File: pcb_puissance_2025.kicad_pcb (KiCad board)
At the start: 2 copper layers, 150 x 90 mm, 120 parts, among them J1 1755736, J10 1755736, J12 1755736, J13 1755736, J14 Conn_02x06_Odd_Even, J15 1755736, J16 1755736, J17 Conn_02x06_Odd_Even, J18 1755736, J19 1755736, J2 1755736, J20 Conn_02x06_Odd_Even, J21 1755736, J22 1755736, J3 1755736, J4 1755736, J5 1755736, J6 1755736, J7 Conn_02x10_Odd_Even, J8 Conn_ST_STDC14, J9 12402012E212A, Q1 SUD50P06-15, Q2 SUD50P06-15, Q3 SUD50P06-15, Q4 SUD50P06-15, Q5 SUD50P06-15, Q6 SUD50P06-15, Q7 STL40DN3LLH5, Q8 NPN, SW1 SW_Push, U1 LTC4417IGN, U10 MCP9808T-E/MS, U2 STM32G491KEU6, U3 INA236BIDDFR, U4 INA236AIDDFR, U5 INA236AIDDFR, U6 INA236AIDDFR, U7 INA236BIDDFR, U8 INA236BIDDFR, U9 TCPP02-M18

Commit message: PCB 2025 rev2
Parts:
- removed J9: 12402012E212A, Modelec:AMPHENOL_12402012E212A
- added J11: USB_C_Receptacle_USB2.0_16P, Modelec:GCT_USB4105-GF-A, B.Cu at (144.2, 145.4)
- added R29: 2k2, Resistor_SMD:R_0805_2012Metric_Pad1.20x1.40mm_HandSolder, B.Cu at (204.4, 141.9)
- added R30: 2k2, Resistor_SMD:R_0805_2012Metric_Pad1.20x1.40mm_HandSolder, B.Cu at (199.8, 141.9)
- added TP1: TestPoint, TestPoint:TestPoint_Pad_D1.5mm, B.Cu at (186.8, 100.0)
- added TP10: TestPoint, TestPoint:TestPoint_Bridge_Pitch2.0mm_Drill0.7mm, B.Cu at (223.5, 74.5)
- added TP2: TestPoint, TestPoint:TestPoint_Pad_D1.5mm, B.Cu at (158.5, 92.0)
- added TP3: TestPoint, TestPoint:TestPoint_Pad_D1.5mm, B.Cu at (189.6, 136.4)
- added TP4: TestPoint, TestPoint:TestPoint_Pad_D1.5mm, B.Cu at (166.5, 79.0)
- added TP5: TestPoint, TestPoint:TestPoint_Pad_D1.5mm, B.Cu at (166.5, 86.5)
- added TP6: TestPoint, TestPoint:TestPoint_Pad_D1.5mm, B.Cu at (166.5, 94.0)
- added TP7: TestPoint, TestPoint:TestPoint_Pad_D1.5mm, B.Cu at (166.5, 101.5)
- added TP8: TestPoint, TestPoint:TestPoint_Pad_D1.5mm, B.Cu at (166.5, 109.0)
- added TP9: TestPoint, TestPoint:TestPoint_Bridge_Pitch2.0mm_Drill0.7mm, B.Cu at (215.5, 72.5)
- C1, C3, C5: value 0.4u -> 0u4
- C11: value 4.7u -> 4u7
- C22: value 2.2u -> 2u2
- R10, R7: value 37.4k -> 37k4
- R11, R8: value 78.7k -> 78k7
- R13, R14, R15: value 8.06k -> 8k06
- R19: value L4CL1206LR013DNR -> 62m 0.5%
- R20, R22: value L4CL1206LR013DNR -> 13m 0.5%
- R21: value L4CL1206LR013DNR -> 20m 0.5%
- R23, R24: value 4m -> 4m 0.5%
- R25: value L4CL1206LR007FNR -> 7m 1%
- R4: value 63.4k -> 63k4
- moved REF** 13.0 mm to (186.0, 84.8)
- moved C23 3.64 mm to (140.2, 88.5), turned to -90 degrees
- moved Q8 0.85 mm to (171.6, 115.8)
- moved R27 0.85 mm to (170.6, 119.5)
- renumbered F6 to F5, F5 to F6
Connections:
- net /Microcontroller/12VALERT renamed /Microcontroller/24VALERT
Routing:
- net GND: track 59.2 -> 117.3 mm, vias 720 -> 743
- net /Microcontroller/SCL: track 296.8 -> 312.5 mm, vias 19 -> 20
- net /3V3: track 378.5 -> 390.7 mm, vias 27 -> 33
- net /Microcontroller/SDA: track 293.7 -> 305.4 mm, vias 17 -> 18
- net Net-(PS1-+VIN_(VCC)): track 21.9 -> 24.2 mm, vias 0 -> 1
- net Net-(BZ1-+): track 5.20 -> 6.30 mm
- net Net-(J11-CC2): track 5.94 -> 6.97 mm
- net /Microcontroller/EMG_PUSHED: track 195.2 -> 196.1 mm
- net Net-(R27-Pad1): track 6.68 -> 7.53 mm
- net Net-(U5-IN-): track 5.12 -> 5.66 mm
- net Net-(U5-IN+): track 5.14 -> 5.68 mm
- net /power_input_selector/VOUT: track 3.47 -> 3.56 mm, vias 1 -> 2
- net Net-(PS3-+VIN_(VCC)): vias 0 -> 1
- net Net-(PS5-+VIN_(VCC)): vias 0 -> 1
- net Net-(PS4-+VIN_(VCC)): vias 0 -> 1
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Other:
- board text added: "12V FUSE"
- board text added: "24V FUSE"
- board text added: "3V3 FUSE"
- board text added: "5V FUSE"
- board text added: "5V15 FUSE"
- board text added: "BUZZER ACTIVATE"
- board text added: "SCL"
- board text added: "SDA"
- board text added: "VIN"
- board text removed: "BIBERON V1 - MARCEL"

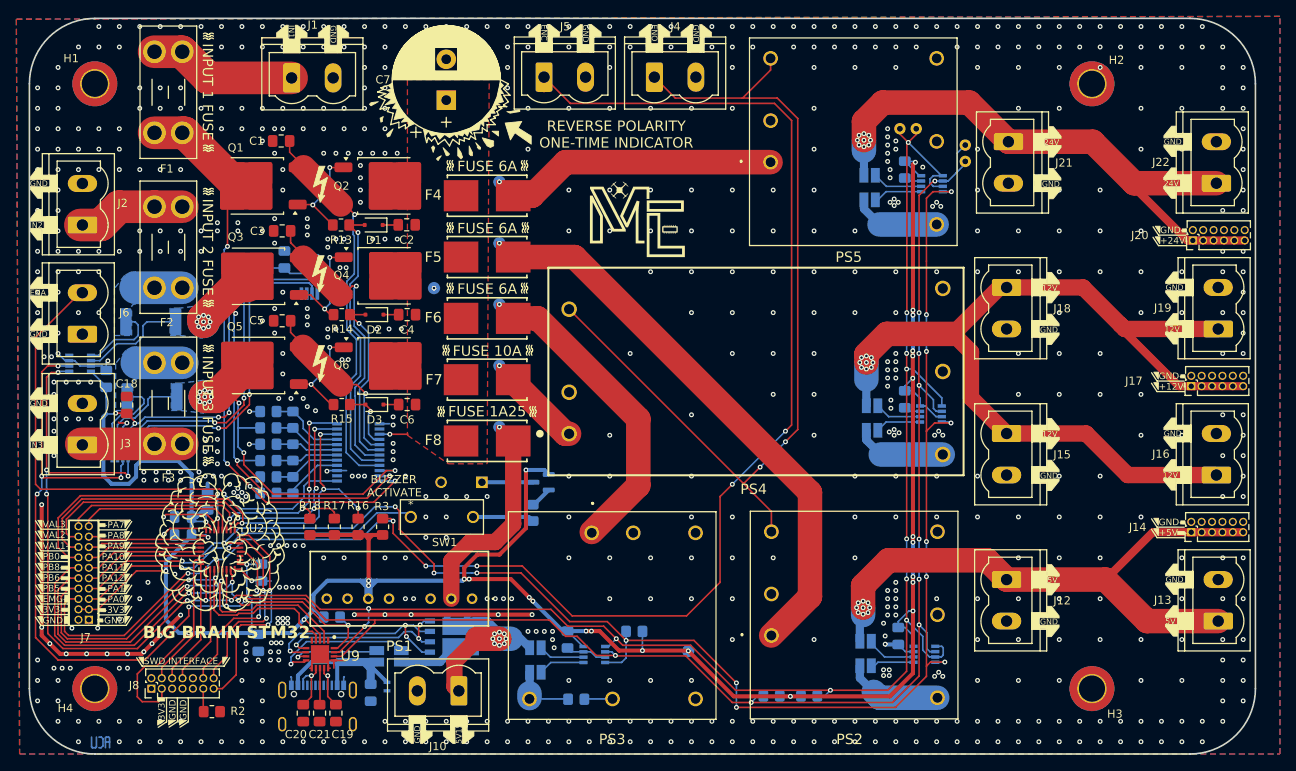
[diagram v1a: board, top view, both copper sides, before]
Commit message: nouvelle version : correction erreurs, ameliorations qualite, passage a 4 couches, ajout pilotage des traco depuis le stm32
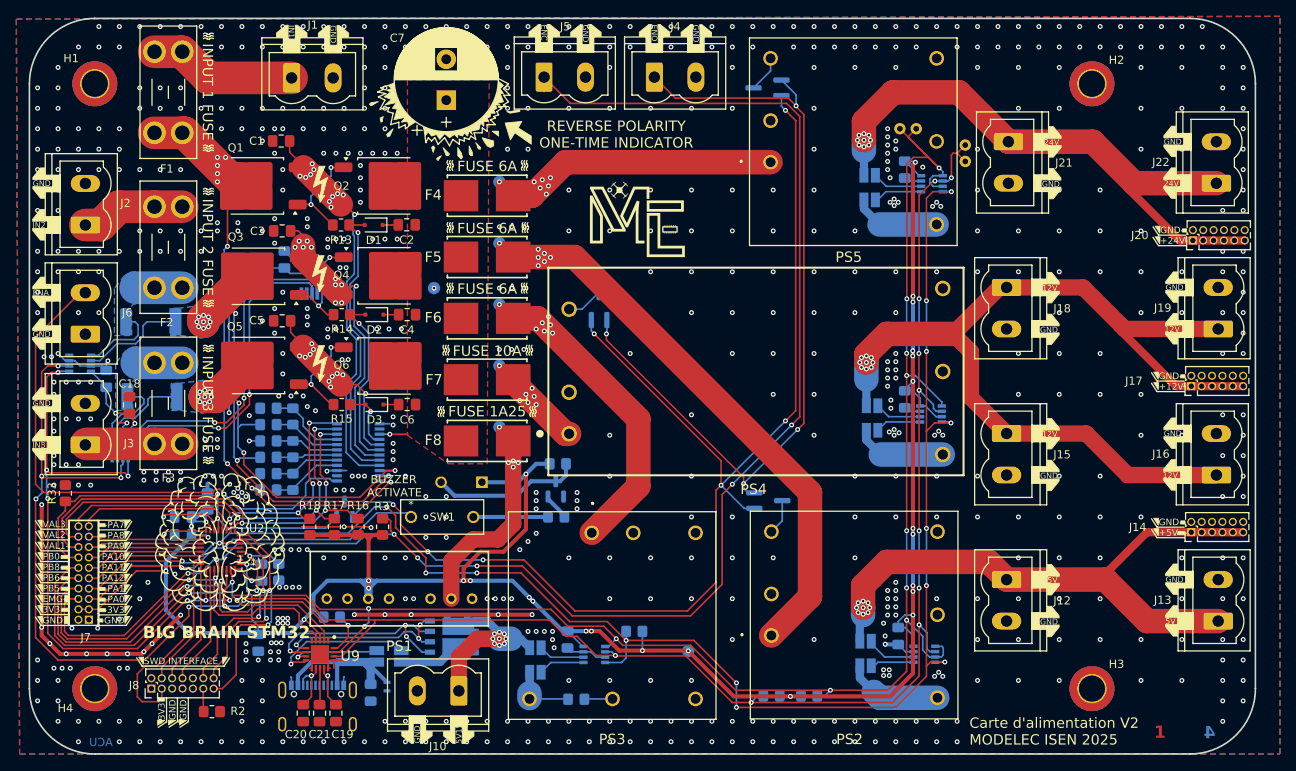
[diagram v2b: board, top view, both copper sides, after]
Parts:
- added D5: D_Dual_CommonAnode_AKK_Parallel, Package_TO_SOT_SMD:TSOT-23_HandSoldering, B.Cu at (199.4, 118.0)
- added D6: D_Dual_CommonAnode_AKK_Parallel, Package_TO_SOT_SMD:TSOT-23_HandSoldering, B.Cu at (178.7, 94.2)
- added D7: D_Dual_CommonAnode_AKK_Parallel, Package_TO_SOT_SMD:TSOT-23_HandSoldering, B.Cu at (199.3, 67.5)
- added Q9: NMOS, Package_TO_SOT_SMD:SOT-23, B.Cu at (147.6, 119.1)
- added R31: 1k, Resistor_SMD:R_0805_2012Metric_Pad1.20x1.40mm_HandSolder, B.Cu at (173.7, 113.5)
- added R32: 1k, Resistor_SMD:R_0805_2012Metric_Pad1.20x1.40mm_HandSolder, B.Cu at (139.5, 126.8)
- added R33: 1k, Resistor_SMD:R_0805_2012Metric_Pad1.20x1.40mm_HandSolder, F.Cu at (113.4, 117.1)
- added REF**: Symbol_HighVoltage_NoTriangle_2x5mm_Copper, Symbol:Symbol_HighVoltage_NoTriangle_2x5mm_Copper, F.Cu at (175.3, 73.4)
- added REF**: Symbol_HighVoltage_NoTriangle_2x5mm_Copper, Symbol:Symbol_HighVoltage_NoTriangle_2x5mm_Copper, F.Cu at (182.3, 71.4)
- added REF**: Symbol_HighVoltage_NoTriangle_2x5mm_Copper, Symbol:Symbol_HighVoltage_NoTriangle_2x5mm_Copper, B.Cu at (174.3, 76.4)
- added REF**: Symbol_HighVoltage_NoTriangle_2x5mm_Copper, Symbol:Symbol_HighVoltage_NoTriangle_2x5mm_Copper, B.Cu at (179.3, 70.4)
- C7: footprint Capacitor_THT:CP_Radial_D13.0mm_P5.00mm -> Capacitor_THT:CP_Radial_D12.5mm_P5.00mm
- moved R27 2.89 mm to (173.4, 120.0), turned to 0 degrees
- moved Q8 1.97 mm to (173.4, 116.6), turned to 90 degrees
- moved REF** 1.88 mm to (187.3, 86.2)
- moved R10 0.40 mm to (138.2, 106.7)
- moved R11 0.40 mm to (141.2, 107.7)
- moved R12 0.40 mm to (138.2, 108.7)
- moved R4 0.40 mm to (138.2, 114.7)
- moved R5 0.40 mm to (141.2, 115.7)
- moved R6 0.40 mm to (138.2, 116.7)
- moved R7 0.40 mm to (138.2, 110.7)
- moved R8 0.40 mm to (141.2, 111.7)
- moved R9 0.40 mm to (138.2, 112.7)
- moved J2 0.36 mm to (115.8, 84.3)
- moved J3 0.36 mm to (115.8, 111.2)
- moved J6 0.36 mm to (115.8, 97.6)
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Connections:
- BZ1 pad 1: Net-(BZ1-+) -> /3V3
- BZ1 pad 2: GND -> Net-(BZ1--)
- J4 pad 1: Net-(PS2-REMOTE_ON/OFF) -> Net-(D5-K-Pad2)
- PS2 pad 6: Net-(PS2-REMOTE_ON/OFF) -> Net-(D5-A)
- PS4 pad 3: Net-(PS2-REMOTE_ON/OFF) -> Net-(D6-A)
- PS4 pad 5: unconnected-(PS4--VOUT-Pad5) -> GND
- PS4 pad 6: GND -> unconnected-(PS4-TRIM-Pad6)
- PS5 pad 6: Net-(PS2-REMOTE_ON/OFF) -> Net-(D7-A)
- Q8 pad 1: /3V3 -> GND
- Q8 pad 3: Net-(BZ1-+) -> Net-(BZ1--)
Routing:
- net /Microcontroller/PWR_CTRL: track 0.00 -> 149.4 mm, vias 0 -> 7
- net Net-(PS2-REMOTE_ON/OFF): track 110.8 -> 0.00 mm, vias 2 -> 0
- net Net-(J17-Pin_1): track 115.8 -> 225.9 mm
- net Net-(D5-K-Pad2): track 0.00 -> 101.4 mm, vias 0 -> 4
- net /3V3: track 390.7 -> 477.0 mm, vias 33 -> 34
- net Net-(J14-Pin_1): track 74.0 -> 144.3 mm
- net Net-(J20-Pin_1): track 72.8 -> 142.5 mm
- net Net-(PS2-+VIN_(VCC)): track 67.7 -> 131.9 mm, vias 1 -> 7
- net Net-(PS3-+VIN_(VCC)): track 36.6 -> 69.3 mm, vias 1 -> 7
- net Net-(PS5-+VIN_(VCC)): track 33.2 -> 62.4 mm, vias 1 -> 7
- net Net-(PS1-+VIN_(VCC)): track 24.2 -> 45.5 mm, vias 1 -> 5
- net Net-(BZ1--): track 0.00 -> 18.4 mm
- net Net-(F1-Pad1): track 18.2 -> 36.3 mm
- net /Microcontroller/PB0: track 31.8 -> 48.1 mm
- net Net-(F2-Pad1): track 13.4 -> 25.6 mm
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- added copper zone on In1.Cu, net GND
- added copper zone on In2.Cu, net GND
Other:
- copper layers 2 -> 4
- board text added: "1"
- board text added: "2"
- board text added: "3"
- board text added: "4"
- board text added: "ACU"
- board text added: "Carte d'alimentation Marcel - MODELEC Documentation : github.com/modelec Dessine par : Allan Cueff Verifie par : Alexandre Jauffrit Version du : 10/02/2025"
- board text added: "Carte d'alimentation V2 MODELEC ISEN 2025"
